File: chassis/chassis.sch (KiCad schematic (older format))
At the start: 27 parts, among them J1 MicroD-15Pins, J10 MicroD-37Pins, J2 MicroD-15Pins, J200 Conn_01x04, J202 Conn_01x07, J203 MilSpec-91Pins, J3 MicroD-37Pins, J4 MicroD-37Pins, J5 MicroD-37Pins, J6 MicroD-37Pins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

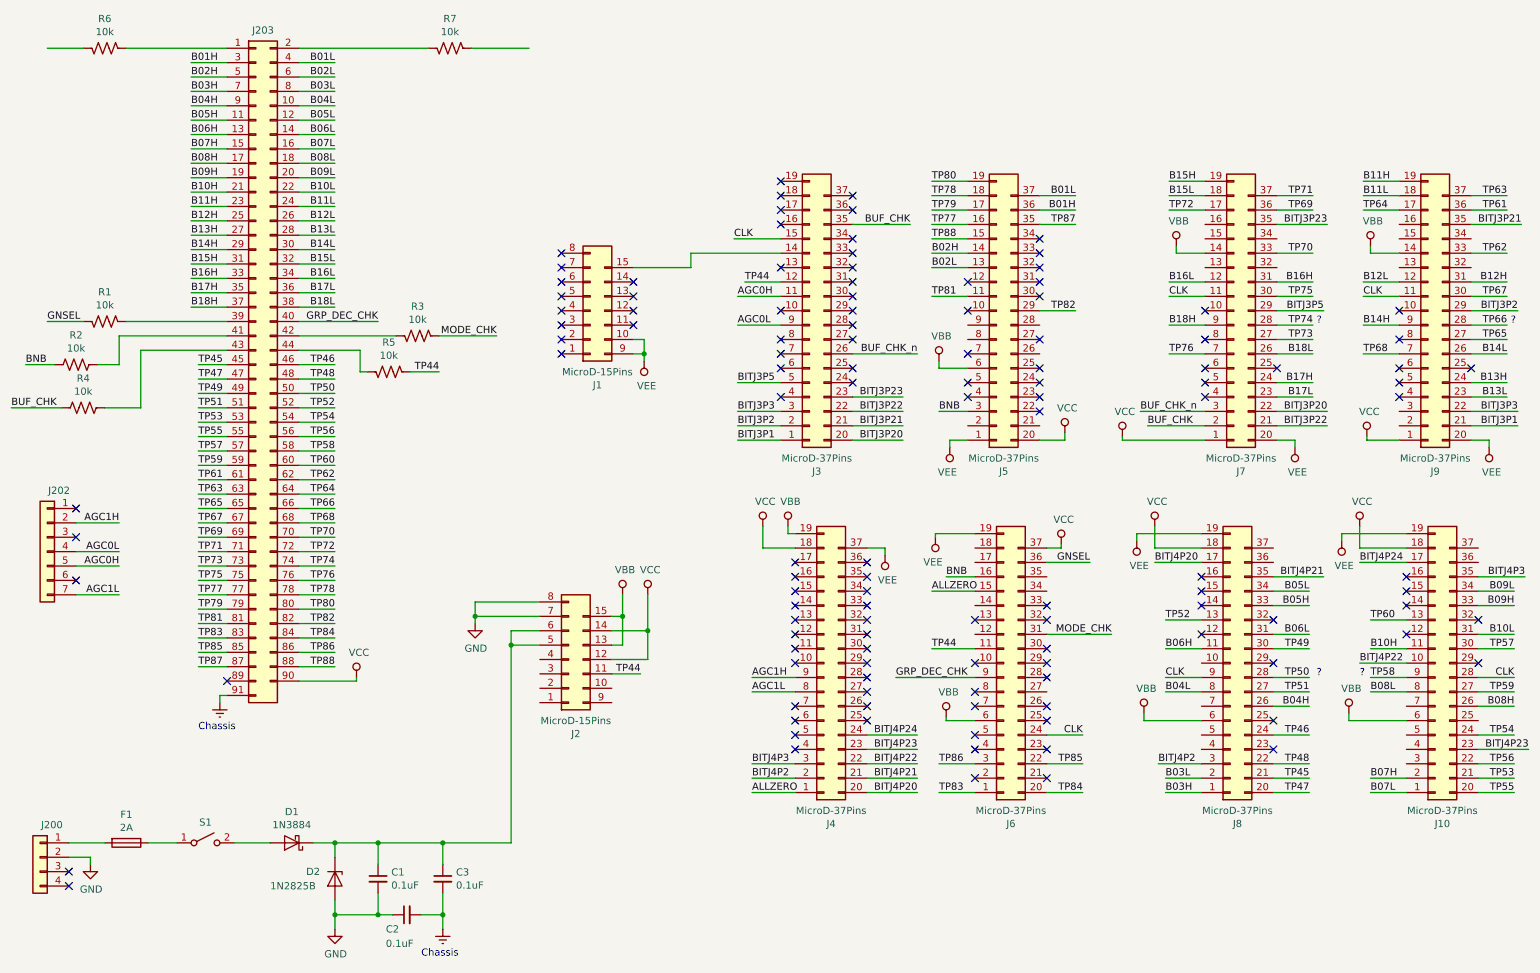
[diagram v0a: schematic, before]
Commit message: Finished mapping out the backplane, barring any connected nets I missed
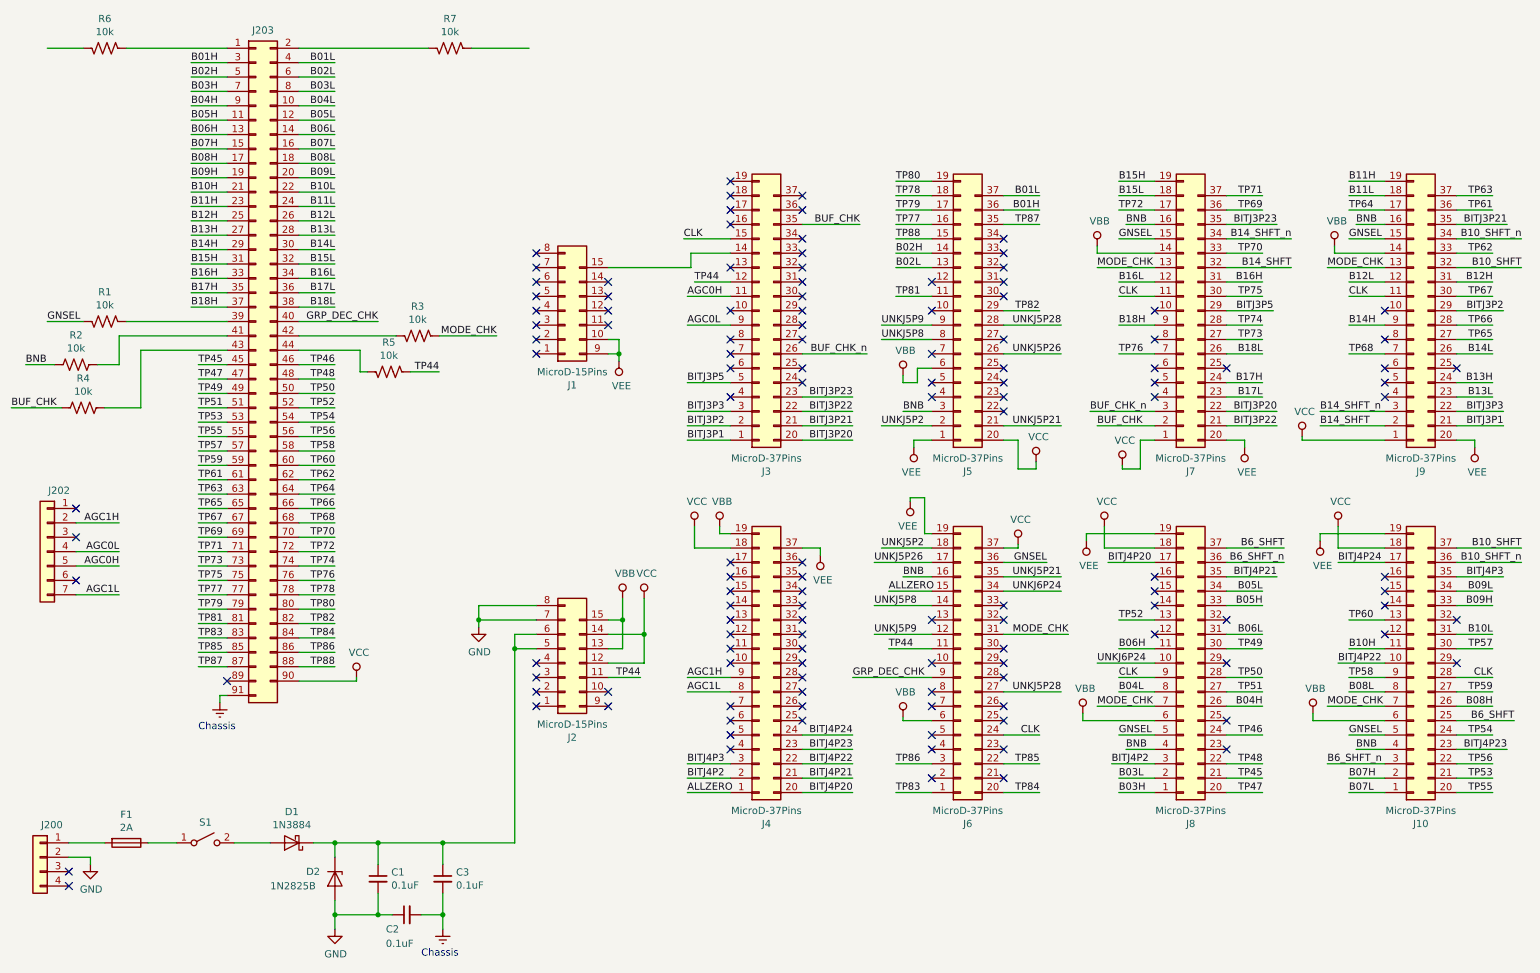
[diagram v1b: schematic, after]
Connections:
- net BNB: now also J10.4 (Pin_4), J7.16 (Pin_16), J8.4 (Pin_4), J9.16 (Pin_16)
- net GNSEL: now also J10.5 (Pin_5), J7.15 (Pin_15), J8.5 (Pin_5), J9.15 (Pin_15)
- net MODE_CHK: now also J10.7 (Pin_7), J7.13 (Pin_13), J8.7 (Pin_7), J9.13 (Pin_13)
- net UNKJ5P2: now reaches J5.2 (Pin_2)
- net UNKJ5P2: now also J6.18 (Pin_18)
- net UNKJ5P21: now reaches J5.21 (Pin_21)
- net UNKJ5P21: now also J6.35 (Pin_35)
- net UNKJ5P26: now reaches J5.26 (Pin_26)
- net UNKJ5P26: now also J6.17 (Pin_17)
- net UNKJ5P28: now reaches J5.28 (Pin_28)
- net UNKJ5P28: now also J6.27 (Pin_27)
- net UNKJ5P8: now reaches J5.8 (Pin_8)
- net UNKJ5P8: now also J6.14 (Pin_14)
- net UNKJ5P9: now reaches J5.9 (Pin_9)
- net UNKJ5P9: now also J6.12 (Pin_12)
- net UNKJ6P24: now reaches J8.10 (Pin_10)
- net UNKJ6P24: now also J6.34 (Pin_34)
- net B6_SHFT_n: now reaches J8.36 (Pin_36)
- net B6_SHFT_n: now also J10.3 (Pin_3)
- net B6_SHFT: now reaches J8.37 (Pin_37)
- net B6_SHFT: now also J10.25 (Pin_25)
- net B10_SHFT_n: now reaches J10.36 (Pin_36)
- net B10_SHFT_n: now also J9.34 (Pin_34)
- net B10_SHFT: now reaches J10.37 (Pin_37)
- net B10_SHFT: now also J9.32 (Pin_32)
- net B14_SHFT: now reaches J9.2 (Pin_2)
- net B14_SHFT: now also J7.32 (Pin_32)
- net B14_SHFT_n: now reaches J9.3 (Pin_3)
- net B14_SHFT_n: now also J7.34 (Pin_34)
- no-connect marks 121 -> 127
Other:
- note removed: "?"
- moved on the sheet: J1, J10, J2, J3, J4, J5, J6, J7, J8, J9
